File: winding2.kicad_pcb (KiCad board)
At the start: 2 copper layers, 15 parts, among them J1 Screw_Terminal_01x06, J2 Screw_Terminal_01x04, J3 Screw_Terminal_01x04, M1 Push_Button_W12mm, SW1 RotaryEncoder_Switch, T1 Push_Button_W12mm, U1 TMC2209_SILENTSTEPSTICK

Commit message: updating the PCB file - still ongoing
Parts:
- removed J1: Screw_Terminal_01x06, Connector_Phoenix_MSTB:PhoenixContact_MSTBA_2,5_6-G-5,08_1x06_P5.08mm_Horizontal
- removed R5: R_Potentiometer_Small, Potentiometer_THT:Potentiometer_Alpha_RD901F-40-00D_Single_Vertical
- removed T1: Push_Button_W12mm, PCM_SL_Devices:Push_Button_W12mm
- added J4: Main Stepper, Connector_Phoenix_MSTB:PhoenixContact_MSTBA_2,5_4-G-5,08_1x04_P5.08mm_Horizontal, F.Cu at (27.6, 69.3)
- added J5: RPM & ESC, Connector_Phoenix_MSTB:PhoenixContact_MSTBA_2,5_4-G-5,08_1x04_P5.08mm_Horizontal, F.Cu at (27.6, 83.8)
- added U2: TMC2209_SILENTSTEPSTICK, TMC2209_SILENTSTEPSTICK:MODULE_TMC2209_SILENTSTEPSTICK, F.Cu at (90.4, 83.0)
- J2: value Screw_Terminal_01x04 -> Limit Switches
- J3: value Screw_Terminal_01x04 -> Screw Stepper
- moved J3 155.1 mm to (27.6, 54.8)
- moved J2 154.7 mm to (27.6, 40.3), turned to 0 degrees
- moved Brd1 124.8 mm to (81.4, 49.7)
- moved A1 121.2 mm to (49.8, 41.8), turned to 0 degrees
- moved R3 113.7 mm to (24.6, 105.0)
- moved U1 113.7 mm to (73.1, 83.0)
- moved R2 112.7 mm to (24.6, 100.9)
- moved R1 112.3 mm to (24.6, 96.9)
- moved BZ1 109.2 mm to (86.2, 100.8)
- moved SW1 66.0 mm to (66.2, 99.1), turned to 0 degrees
- moved M1 55.2 mm to (55.8, 92.7)
- moved D1 54.4 mm to (55.8, 78.9)
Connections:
- A1 pad 22: unconnected-(A1-A2-Pad22) -> /DIR2
- A1 pad 23: unconnected-(A1-A3-Pad23) -> /STP2
- U1 pad 10: unconnected-(U1-STEP-Pad10) -> /STP2
- U1 pad 16: unconnected-(U1-~{EN}-Pad16) -> GND
- U1 pad 2: unconnected-(U1-VIO-Pad2) -> 5V
- U1 pad 9: unconnected-(U1-DIR-Pad9) -> /DIR2
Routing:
- net GND: track 22.0 -> 0.00 mm
- net 5V: track 16.3 -> 0.00 mm

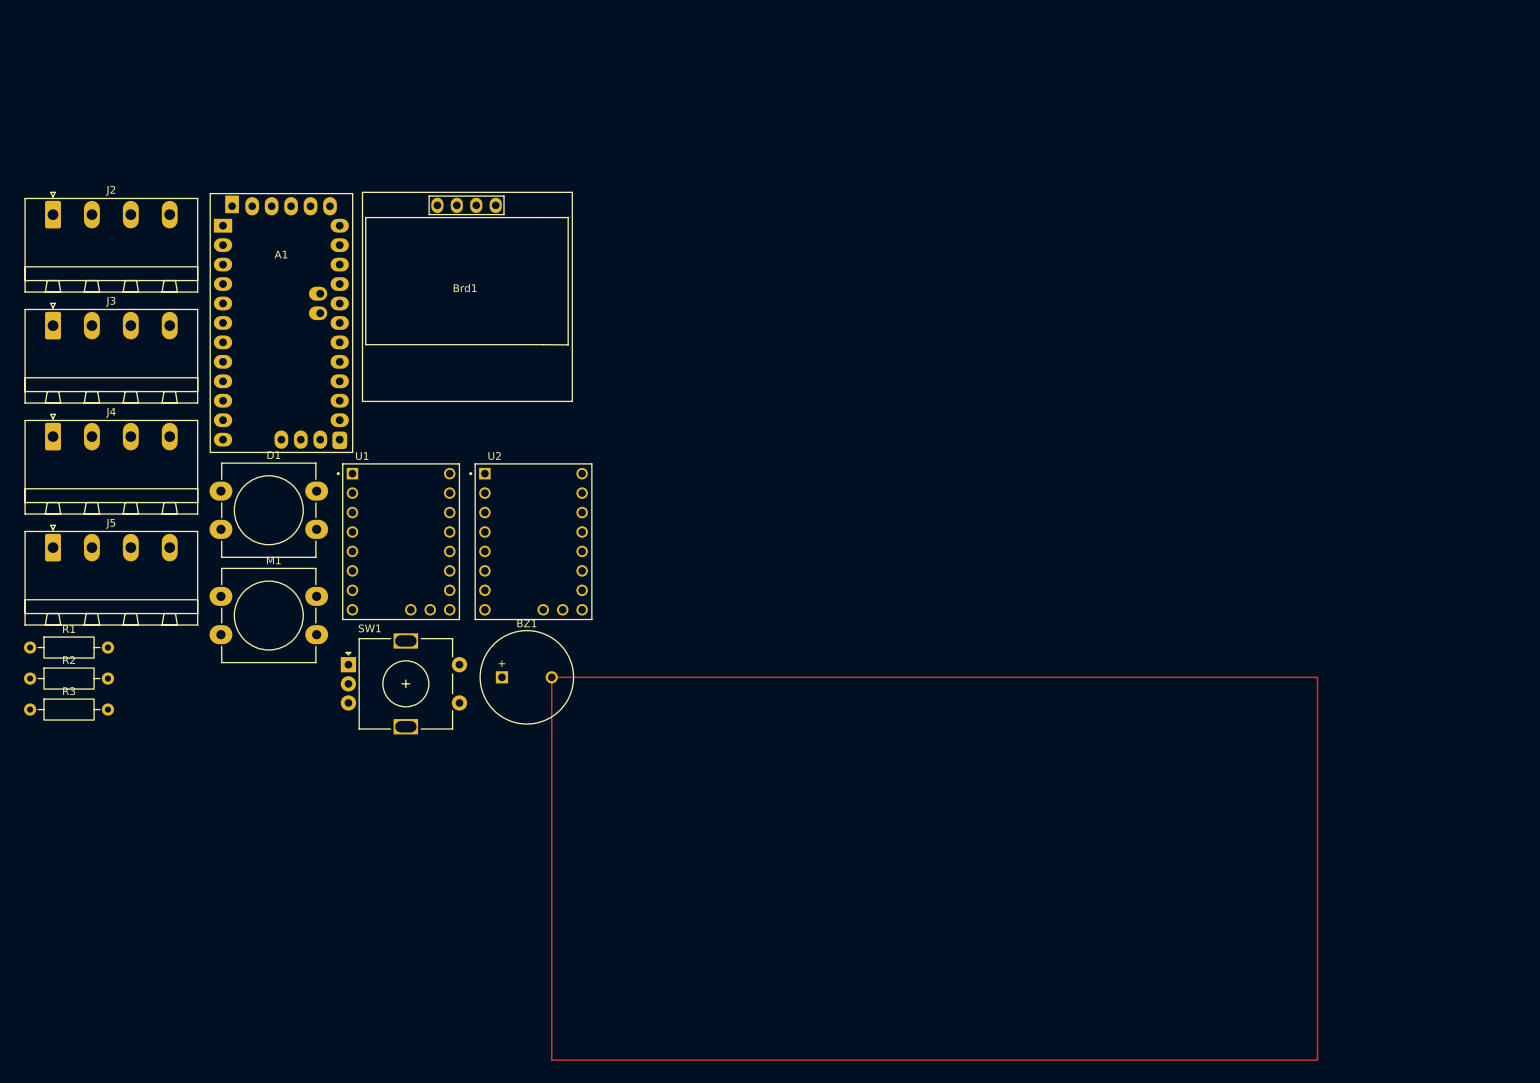
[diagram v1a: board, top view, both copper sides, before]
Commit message: finalize the schematic part and footprints assigning step
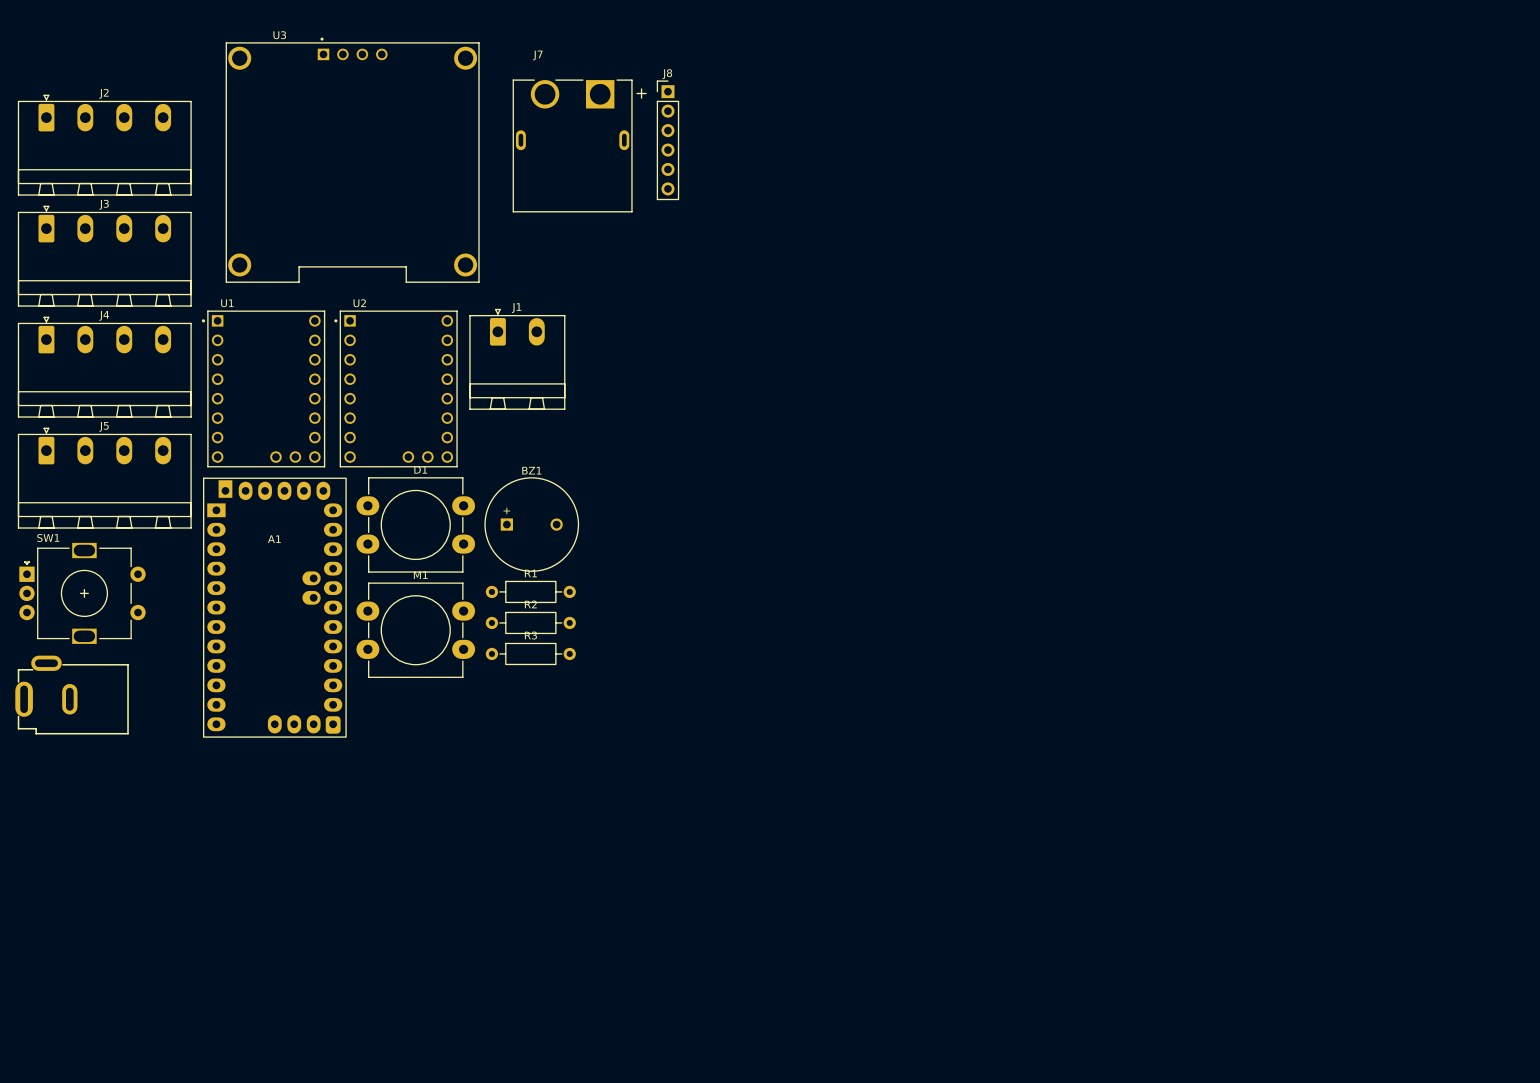
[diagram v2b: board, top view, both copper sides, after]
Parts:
- removed Brd1: SSD1306, SSD1306:128x64OLED
- added J1: Screw_Terminal_2_P5.00mm, Connector_Phoenix_MSTB:PhoenixContact_MSTBA_2,5_2-G-5,08_1x02_P5.08mm_Horizontal, F.Cu at (85.7, 55.6)
- added J6: Barrel_Jack_PTH_Slot, PCM_SparkFun-Connector:Barrel_Jack_PTH_Slot, F.Cu at (29.8, 103.6)
- added J7: ESC XT60-F, XT60PW-F:AMASS_XT60PW-F, F.Cu at (95.5, 24.6)
- added J8: ARDUINO PROG., Connector_PinHeader_2.54mm:PinHeader_1x06_P2.54mm_Vertical, F.Cu at (107.9, 24.3)
- added U3: DM-OLED096-636, DM-OLED096-636:MODULE_DM-OLED096-636, F.Cu at (66.8, 30.9)
- moved R1 60.7 mm to (84.9, 89.6)
- moved R2 60.7 mm to (84.9, 93.7)
- moved R3 60.7 mm to (84.9, 97.7)
- moved SW1 43.6 mm to (24.2, 87.3)
- moved A1 37.2 mm to (49.0, 78.9)
- moved U1 26.6 mm to (55.5, 63.1)
- moved U2 26.6 mm to (72.8, 63.1)
- moved BZ1 20.0 mm to (86.9, 80.8)
- moved D1 19.3 mm to (75.0, 80.8)
- moved M1 19.3 mm to (75.0, 94.6)
- moved J2 12.7 mm to (26.8, 27.7)
- moved J3 12.7 mm to (26.8, 42.1)
- moved J5 12.7 mm to (26.8, 71.1)
- moved J4 12.7 mm to (26.8, 56.6)
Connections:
- A1 pad 1: unconnected-(A1-1/TX-Pad1)_1 -> /Ard_Tx
- A1 pad 2: unconnected-(A1-0/RX-Pad2) -> /Ard_Rx
- A1 pad 24: unconnected-(A1-VCC-Pad24) -> 5V
- A1 pad 28: unconnected-(A1-GND-Pad28) -> GND
- A1 pad 31: unconnected-(A1-DTR-Pad31) -> /DTR
- U1 pad 8: unconnected-(U1-VM-Pad8) -> /16V
- U2 pad 3: unconnected-(U2-M1B-Pad3) -> /M1B
- U2 pad 4: unconnected-(U2-M1A-Pad4) -> /M1A
- U2 pad 5: unconnected-(U2-M2A-Pad5) -> /M2A
- U2 pad 6: unconnected-(U2-M2B-Pad6) -> /M2B
- U2 pad 8: unconnected-(U2-VM-Pad8) -> /16V

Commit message: editing the OLED screen footprint
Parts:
- moved U3 1.15 mm to (66.8, 32.0)

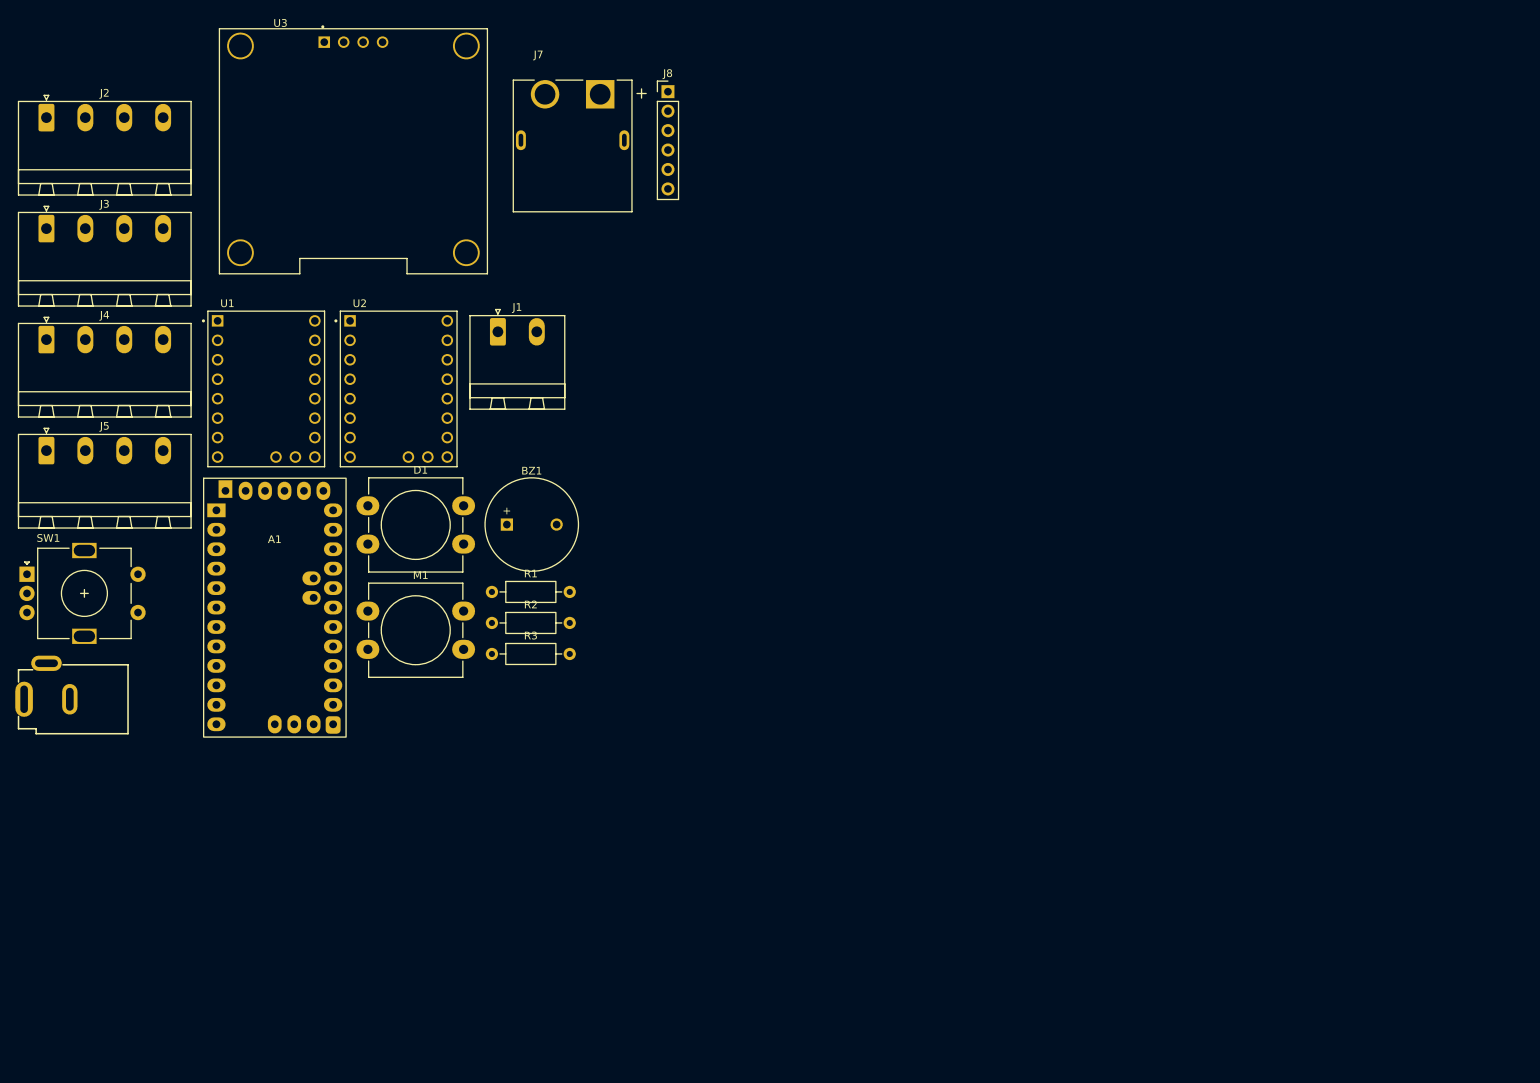
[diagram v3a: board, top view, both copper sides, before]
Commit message: initial placing and layout of components
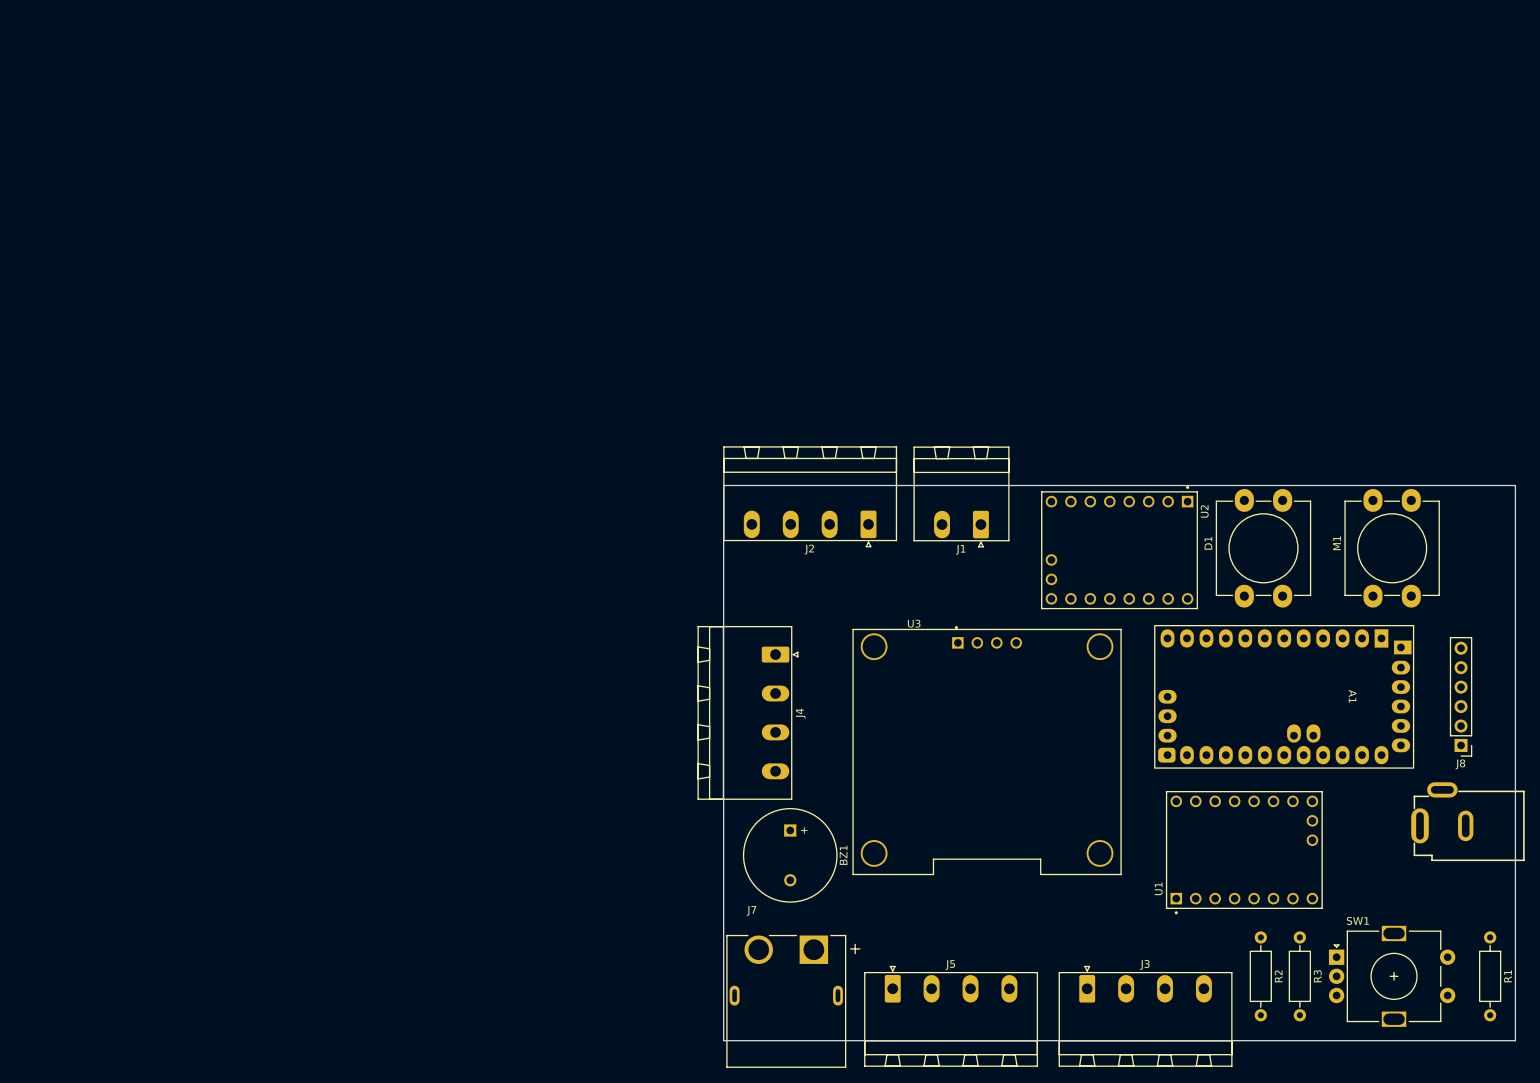
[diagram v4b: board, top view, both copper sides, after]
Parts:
- moved J6 183.0 mm to (212.1, 120.1)
- moved SW1 178.2 mm to (195.2, 137.3)
- moved J3 168.3 mm to (162.7, 141.4)
- moved A1 153.1 mm to (201.1, 95.7), turned to -90 degrees
- moved U1 141.2 mm to (183.2, 123.3), turned to 90 degrees
- moved R1 137.9 mm to (215.3, 134.7), turned to -90 degrees
- moved J8 134.2 mm to (211.5, 109.7), turned to 180 degrees
- moved J5 131.0 mm to (137.3, 141.4)
- moved M1 128.0 mm to (202.5, 83.9), turned to 90 degrees
- moved J2 119.8 mm to (134.1, 80.8), turned to 180 degrees
- moved J7 115.1 mm to (123.4, 136.3)
- moved U3 114.0 mm to (149.6, 110.5)
- moved R3 111.8 mm to (190.4, 134.7), turned to -90 degrees
- moved D1 110.8 mm to (185.7, 83.9), turned to 90 degrees
- moved R2 108.5 mm to (185.3, 134.7), turned to -90 degrees
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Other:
- board outline added: 103.4 x 72.5 mm

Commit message: trial: testing the free router plugin
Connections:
- J3 pad 1: unconnected-(J3-Pin_1-Pad1) -> /S1B
- J3 pad 2: unconnected-(J3-Pin_2-Pad2) -> /S1A
- J3 pad 3: unconnected-(J3-Pin_3-Pad3) -> /S2A
- J3 pad 4: unconnected-(J3-Pin_4-Pad4) -> /S2B
- J4 pad 1: unconnected-(J4-Pin_1-Pad1) -> /M1B
- J4 pad 2: unconnected-(J4-Pin_2-Pad2) -> /M1A
- J4 pad 3: unconnected-(J4-Pin_3-Pad3) -> /M2A
- J4 pad 4: unconnected-(J4-Pin_4-Pad4) -> /M2B
- U1 pad 3: unconnected-(U1-M1B-Pad3) -> /S1B
- U1 pad 4: unconnected-(U1-M1A-Pad4) -> /S1A
- U1 pad 5: unconnected-(U1-M2A-Pad5) -> /S2A
- U1 pad 6: unconnected-(U1-M2B-Pad6) -> /S2B
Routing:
- net GND: track 0.00 -> 365.5 mm, vias 0 -> 1
- net 5V: track 0.00 -> 271.5 mm, vias 0 -> 1
- net /16V: track 0.00 -> 162.7 mm, vias 0 -> 1
- net /limit1: track 0.00 -> 100.2 mm
- net /OLED-A5: track 0.00 -> 82.6 mm
- net /RPM: track 0.00 -> 77.9 mm, vias 0 -> 1
- net /M2B: track 0.00 -> 73.3 mm, vias 0 -> 1
- net /M2A: track 0.00 -> 73.1 mm, vias 0 -> 1
- net /M1A: track 0.00 -> 71.0 mm, vias 0 -> 1
- net /limit2: track 0.00 -> 68.0 mm
- net /BUZZ-A0: track 0.00 -> 65.6 mm, vias 0 -> 2
- net /M1B: track 0.00 -> 64.1 mm, vias 0 -> 1
- net /ESC-S: track 0.00 -> 56.2 mm
- net /ENCODER_SW: track 0.00 -> 56.2 mm
- net /OLED-A4: track 0.00 -> 55.7 mm
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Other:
- board size 103.4 x 72.5 mm -> 103.4 x 74.2 mm
